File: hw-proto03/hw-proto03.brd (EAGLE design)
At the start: 87.3 x 69.8 mm, 43 parts, among them IC1 TLV74333PDBVR, IC2 IR4427S, IC3 MCP2562T, IC5 IR4427S, J1 J12MM, J2 J5MM, J3 J12MM, J4 J7MM, Q1 SQJ147ELP-T1_GE3, Q2 SQJ147ELP-T1_GE3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

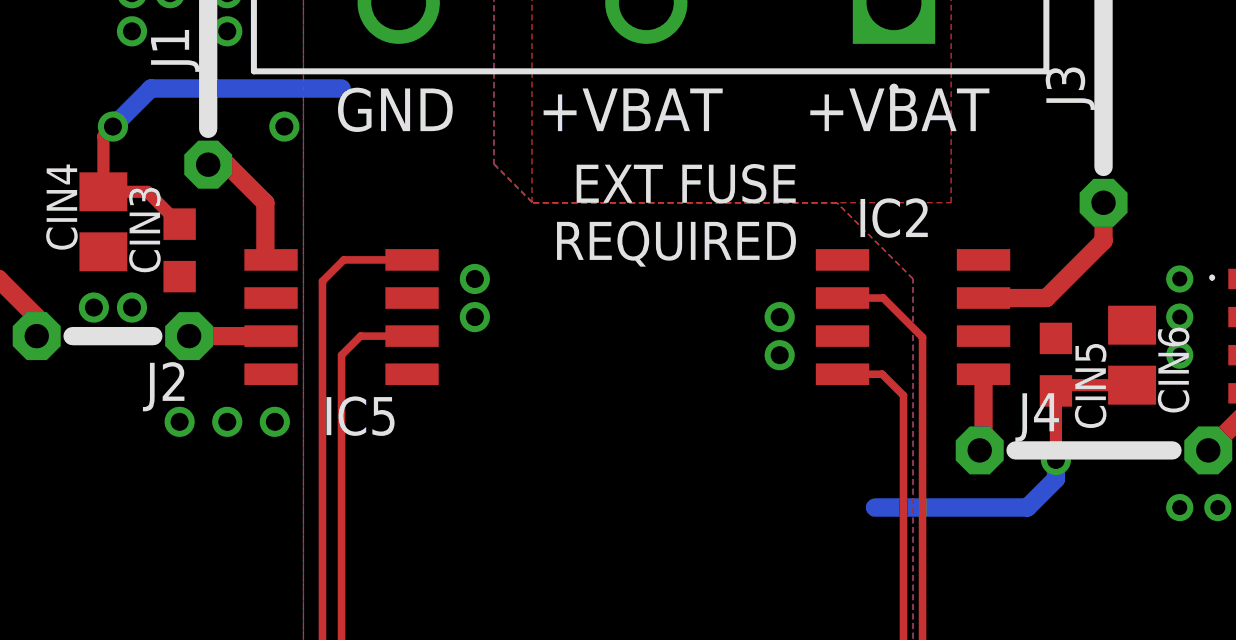
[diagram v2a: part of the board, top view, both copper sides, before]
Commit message: updated new fet driver
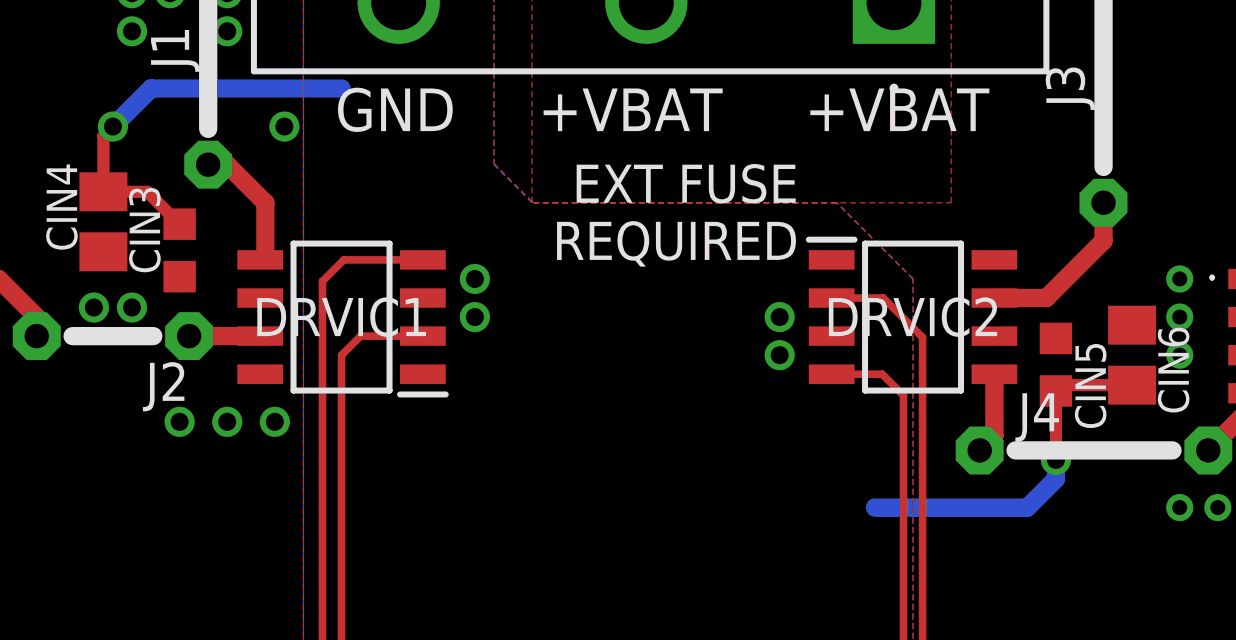
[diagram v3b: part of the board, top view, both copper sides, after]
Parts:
- removed IC2, IC5: IR4427S, ir:SO08
- added DRVIC1, DRVIC2: UCC27523DR, UCC27523DR-fet-driver:SOIC127P600X175-8N
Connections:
- net +12V: now also DRVIC1.6, DRVIC2.6; no longer IC2.6, IC5.6
- net CTL1: now also DRVIC1.4; no longer IC5.4
- net CTL2: now also DRVIC1.2; no longer IC5.2
- net CTL4: now also DRVIC2.2; no longer IC2.2
- net CTL5: now also DRVIC2.4; no longer IC2.4
- net GND: now also DRVIC1.3, DRVIC2.3; no longer IC2.3, IC5.3
- net N$13: now also DRVIC1.7; no longer IC5.7
- net N$4: now also DRVIC1.5; no longer IC5.5
- net N$8: now also DRVIC2.5; no longer IC2.5
- net N$9: now also DRVIC2.7; no longer IC2.7
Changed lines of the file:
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@@
 <attribute name="NAME" x="14.6342" y="11.5878" size="1.27" layer="25" ratio="10"/>
-</element>
-<element name="IC5" library="ir" package="SO08" value="IR4427S" x="36.83" y="48.26" rot="R90">
-<attribute name="OC_FARNELL" value="8639094" x="36.83" y="48.26" size="1.778" layer="27" rot="R90" display="off"/>
-<attribute name="MPN" value="IR4427STRPBF" x="36.83" y="48.26" size="1.778" layer="27" rot="R90" display="off"/>
-<attribute name="MF" value="INTERNATIONAL RECTIFIER(IR)" x="36.83" y="48.26" size="1.778" layer="27" rot="R90" display="off"/>
-<attribute name="OC_NEWARK" value="63J7933" x="36.83" y="48.26" size="1.778" layer="27" rot="R90" display="off"/>
 </element>
 <element name="R1" library="rcl" package="0204/7" value="10K0" x="29.5275" y="30.7975" rot="R180"/>
@@
 <element name="CIN2" library="rcl" package="C0603K" value="100n" x="65.0875" y="6.0325" rot="R270"/>
 <element name="CEN" library="rcl" package="C0603K" value="1u" x="65.0875" y="13.6525" rot="R90"/>
-<element name="IC2" library="ir" package="SO08" value="IR4427S" x="55.88" y="48.26" rot="R270">
-<attribute name="MF" value="INTERNATIONAL RECTIFIER(IR)" x="74.93" y="48.26" size="1.778" layer="27" rot="R270" display="off"/>
-<attribute name="OC_NEWARK" value="63J7933" x="74.93" y="48.26" size="1.778" layer="27" rot="R270" display="off"/>
-<attribute name="MPN" value="IR4427STRPBF" x="74.93" y="48.26" size="1.778" layer="27" rot="R270" display="off"/>
-<attribute name="OC_FARNELL" value="8639094" x="74.93" y="48.26" size="1.778" layer="27" rot="R270" display="off"/>
-</element>
 <element name="Q4" library="transistor-vishay-pchan-pso8" package="SQJ147ELPT1_GE3" value="SQJ147ELP-T1_GE3" x="69.85" y="64.135" rot="R270">
 <attribute name="DESCRIPTION" value="MOSFET P-CHANNEL 40-V (D-S) 175C MOSFET" x="63.5" y="78.105" size="1.778" layer="27" rot="R270" display="off"/>
@@
 <element name="CIN5" library="rcl" package="C0603K" value="100n" x="60.6425" y="46.6725" rot="R270"/>
 <element name="CIN6" library="rcl" package="C0805K" value="4u7" x="63.1825" y="46.99" rot="R270"/>
+<element name="DRVIC1" library="UCC27523DR-fet-driver" package="SOIC127P600X175-8N" value="UCC27523DR" x="36.83" y="48.26" rot="R180">
+<attribute name="MOUSER_PART_NUMBER" value="595-UCC27523DR" x="36.83" y="48.26" size="1.778" layer="27" rot="R180" display="off"/>
+<attribute name="MANUFACTURER_NAME" value="Texas Instruments" x="36.83" y="48.26" size="1.778" layer="27" rot="R180" display="off"/>
+<attribute name="MANUFACTURER_PART_NUMBER" value="UCC27523DR" x="36.83" y="48.26" size="1.778" layer="27" rot="R180" display="off"/>
+<attribute name="MOUSER_PRICE-STOCK" value="https://www.mouser.co.uk/ProductDetail/Texas-Instruments/UCC27523DR/?qs=JK0Mn6q9DKQ5jNt3UHw5hw%3D%3D" x="36.83" y="48.26" size="1.778" layer="27" rot="R180" display="off"/>
+<attribute name="DESCRIPTION" value="Dual, 5A, High-Speed Low-Side Power MOSFET Driver" x="36.83" y="48.26" size="1.778" layer="27" rot="R180" display="off"/>
+<attribute name="HEIGHT" value="1.75mm" x="36.83" y="48.26" size="1.778" layer="27" rot="R180" display="off"/>
+</element>
+<element name="DRVIC2" library="UCC27523DR-fet-driver" package="SOIC127P600X175-8N" value="UCC27523DR" x="55.88" y="48.26">
+<attribute name="MOUSER_PART_NUMBER" value="595-UCC27523DR" x="55.88" y="48.26" size="1.778" layer="27" display="off"/>
+<attribute name="MANUFACTURER_NAME" value="Texas Instruments" x="55.88" y="48.26" size="1.778" layer="27" display="off"/>
+<attribute name="MANUFACTURER_PART_NUMBER" value="UCC27523DR" x="55.88" y="48.26" size="1.778" layer="27" display="off"/>
+<attribute name="MOUSER_PRICE-STOCK" value="https://www.mouser.co.uk/ProductDetail/Texas-Instruments/UCC27523DR/?qs=JK0Mn6q9DKQ5jNt3UHw5hw%3D%3D" x="55.88" y="48.26" size="1.778" layer="27" display="off"/>
+<attribute name="DESCRIPTION" value="Dual, 5A, High-Speed Low-Side Power MOSFET Driver" x="55.88" y="48.26" size="1.778" layer="27" display="off"/>
+<attribute name="HEIGHT" value="1.75mm" x="55.88" y="48.26" size="1.778" layer="27" display="off"/>
+</element>
 </elements>
 <signals>
@@
 <vertex x="1.27" y="1.27"/>
 </polygon>
-<contactref element="IC5" pad="3"/>
 <polygon width="0.4064" layer="1" spacing="0.3048" isolate="0.254" rank="6">
 <vertex x="1.27" y="71.12"/>
@@
 <via x="67.6275" y="11.1125" extent="1-16" drill="0.5"/>
 <via x="68.8975" y="11.1125" extent="1-16" drill="0.5"/>
-<contactref element="IC2" pad="3"/>
 <contactref element="PWRIN" pad="3"/>
 <contactref element="PWR1" pad="2"/>
@@
 <wire x1="31.4325" y1="51.3575" x2="30.355" y2="52.435" width="0.4064" layer="1"/>
 <wire x1="30.355" y1="52.435" x2="28.8925" y2="52.435" width="0.4064" layer="1"/>
+<contactref element="DRVIC1" pad="3"/>
+<contactref element="DRVIC2" pad="3"/>
 </signal>
 <signal name="SW1">
@@
 <contactref element="Q3" pad="5"/>
 <contactref element="Q3" pad="8"/>
-<contactref element="IC5" pad="6"/>
 <contactref element="Q1" pad="3"/>
 <contactref element="Q1" pad="2"/>
@@
 <contactref element="Q2" pad="2"/>
 <contactref element="Q2" pad="3"/>
-<contactref element="IC2" pad="6"/>
 <contactref element="Q4" pad="3"/>
 <contactref element="Q4" pad="2"/>
@@
 <via x="33.02" y="44.7675" extent="1-16" drill="0.6"/>
 <via x="31.4325" y="44.7675" extent="1-16" drill="0.6"/>
+<contactref element="DRVIC1" pad="6"/>
+<contactref element="DRVIC2" pad="6"/>
 </signal>
 <signal name="+5V">
@@
 </signal>
 <signal name="CTL4">
-<contactref element="IC2" pad="2"/>
 <contactref element="MCU" pad="12"/>
-<wire x1="53.53" y1="48.895" x2="54.888415625" y2="48.895" width="0.254" layer="1"/>
 <wire x1="54.888415625" y1="48.895" x2="56.1975" y2="47.585915625" width="0.254" layer="1"/>
 <wire x1="56.1975" y1="47.585915625" x2="56.1975" y2="32.7025" width="0.254" layer="1"/>
@@
 <via x="57.15" y="19.05" extent="1-16" drill="0.6" shape="octagon"/>
 <wire x1="57.15" y1="19.05" x2="57.15" y2="31.75" width="0.254" layer="16"/>
+<contactref element="DRVIC2" pad="2"/>
+<wire x1="53.168" y1="48.895" x2="54.888415625" y2="48.895" width="0.254" layer="1"/>
 </signal>
 <signal name="CTL3">
@@
 </signal>
 <signal name="N$4">
-<contactref element="IC5" pad="5"/>
 <contactref element="J1" pad="1"/>
 <wire x1="32.385" y1="53.34" x2="33.02" y2="53.34" width="0.6096" layer="1"/>
 <wire x1="33.02" y1="53.34" x2="34.29" y2="52.07" width="0.6096" layer="1"/>
-<wire x1="34.29" y1="52.07" x2="34.29" y2="50.355" width="0.6096" layer="1"/>
-<wire x1="34.29" y1="50.355" x2="34.48" y2="50.165" width="0.6096" layer="1"/>
+<contactref element="DRVIC1" pad="5"/>
+<wire x1="34.29" y1="52.07" x2="34.29" y2="50.337" width="0.6096" layer="1"/>
+<wire x1="34.29" y1="50.337" x2="34.118" y2="50.165" width="0.6096" layer="1"/>
 </signal>
 <signal name="CTL2">
-<contactref element="IC5" pad="2"/>
 <wire x1="42.09" y1="20.14" x2="36.83" y2="25.4" width="0.254" layer="1"/>
-<wire x1="39.18" y1="47.625" x2="37.465" y2="47.625" width="0.254" layer="1"/>
 <wire x1="37.465" y1="47.625" x2="36.83" y2="46.99" width="0.254" layer="1"/>
 <wire x1="36.83" y1="46.99" x2="36.83" y2="25.4" width="0.254" layer="1"/>
 <contactref element="MCU" pad="26"/>
 <wire x1="43.32" y1="20.14" x2="42.09" y2="20.14" width="0.254" layer="1"/>
+<contactref element="DRVIC1" pad="2"/>
+<wire x1="39.542" y1="47.625" x2="37.465" y2="47.625" width="0.254" layer="1"/>
 </signal>
 <signal name="CTL1">
-<contactref element="IC5" pad="4"/>
 <wire x1="36.195" y1="20.955" x2="36.195" y2="49.45505" width="0.254" layer="1"/>
 <wire x1="36.195" y1="49.45505" x2="36.90495" y2="50.165" width="0.254" layer="1"/>
-<wire x1="36.90495" y1="50.165" x2="39.18" y2="50.165" width="0.254" layer="1"/>
 <wire x1="36.195" y1="20.955" x2="42.09" y2="15.06" width="0.254" layer="1"/>
 <contactref element="MCU" pad="30"/>
 <wire x1="43.32" y1="15.06" x2="42.09" y2="15.06" width="0.254" layer="1"/>
+<contactref element="DRVIC1" pad="4"/>
+<wire x1="36.90495" y1="50.165" x2="39.542" y2="50.165" width="0.254" layer="1"/>
 </signal>
 <signal name="CAN_TX">
@@
 </signal>
 <signal name="N$8">
-<contactref element="IC2" pad="5"/>
 <contactref element="J4" pad="1"/>
-<wire x1="58.23" y1="46.355" x2="58.23" y2="43.9425" width="0.6096" layer="1"/>
 <wire x1="58.23" y1="43.9425" x2="58.1025" y2="43.815" width="0.6096" layer="1"/>
+<contactref element="DRVIC2" pad="5"/>
+<wire x1="58.592" y1="46.355" x2="58.592" y2="44.3045" width="0.6096" layer="1"/>
+<wire x1="58.592" y1="44.3045" x2="58.1025" y2="43.815" width="0.6096" layer="1"/>
 </signal>
 <signal name="N$9">
-<contactref element="IC2" pad="7"/>
 <contactref element="J3" pad="1"/>
-<wire x1="58.23" y1="48.895" x2="60.325" y2="48.895" width="0.6096" layer="1"/>
 <wire x1="60.325" y1="48.895" x2="62.23" y2="50.8" width="0.6096" layer="1"/>
 <wire x1="62.23" y1="52.07" x2="62.23" y2="50.8" width="0.6096" layer="1"/>
+<contactref element="DRVIC2" pad="7"/>
+<wire x1="60.325" y1="48.895" x2="58.592" y2="48.895" width="0.6096" layer="1"/>
 </signal>
 <signal name="N$10">
@@
 </signal>
 <signal name="CTL5">
-<contactref element="IC2" pad="4"/>
 <contactref element="MCU" pad="11"/>
-<wire x1="53.53" y1="46.355" x2="54.85255" y2="46.355" width="0.254" layer="1"/>
 <wire x1="54.85255" y1="46.355" x2="55.5625" y2="45.64505" width="0.254" layer="1"/>
 <wire x1="55.5625" y1="45.64505" x2="55.5625" y2="28.8925" width="0.254" layer="1"/>
@@
 <via x="54.61" y="17.78" extent="1-16" drill="0.6" shape="octagon"/>
 <wire x1="54.61" y1="17.78" x2="54.61" y2="27.94" width="0.254" layer="16"/>
+<contactref element="DRVIC2" pad="4"/>
+<wire x1="53.168" y1="46.355" x2="54.85255" y2="46.355" width="0.254" layer="1"/>
 </signal>
 <signal name="N$13">
-<contactref element="IC5" pad="7"/>
 <contactref element="J2" pad="1"/>
-<wire x1="34.48" y1="47.625" x2="31.75" y2="47.625" width="0.6096" layer="1"/>
+<contactref element="DRVIC1" pad="7"/>
+<wire x1="34.118" y1="47.625" x2="31.75" y2="47.625" width="0.6096" layer="1"/>
 </signal>
 <signal name="CANSTBY">
